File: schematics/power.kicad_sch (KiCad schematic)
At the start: 42 parts, among them J1 9VRMS 60HZ AC, SW1 SW_SPDT, SW2 SW_Push, SW3 SW_Push, SW4 SW_Push, U1 74HC14, U2 LM2576T-ADJ, U3 LM317T, U5 74HC08

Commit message: adjusted some input voltages
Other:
- note added: "+4V5"
- note added: "measured 10V6RMS"
- note added: "~+12V6"
- note removed: "+6V3"
- note removed: "~+10V"
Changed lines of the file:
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@@
 	(generator_version "10.0")
 	(paper "USLetter")
-	(text "~+10V"
+	(text "~+12V6"
 		(exclude_from_sim no)
 		(at 100.33 53.34 0)
@@
 			)
 			(justify left bottom)
+		)
+	)
+	(text "measured 10V6RMS"
+		(exclude_from_sim no)
+		(at 77.47 46.99 0)
+		(effects
+			(font
+				(size 1.27 1.27)
+			)
+			(justify right)
 		)
 	)
@@
 		)
 	)
-	(text "+6V3"
+	(text "+4V5"
 		(exclude_from_sim no)
 		(at 135.89 53.34 0)

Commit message: started a second version
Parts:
- removed C10: 10U, Package_SO:SOIC-8_3.9x4.9mm_P1.27mm, symbol Device:C
- removed C11: 1U, Package_SO:SOIC-8_3.9x4.9mm_P1.27mm, symbol Device:C
- removed C3: 330N, Package_SO:SOIC-8_3.9x4.9mm_P1.27mm, symbol Device:C
- removed C8: 100N, Package_SO:SOIC-8_3.9x4.9mm_P1.27mm, symbol Device:C
- removed D7, D8: 1N4007, Diode_THT:D_DO-35_SOD27_P7.62mm_Horizontal, symbol Diode:1N4148
- removed R36: 22K, symbol Device:R
- removed RV2: 5K, Package_SO:TSSOP-20_4.4x6.5mm_P0.65mm, symbol Device:R_Potentiometer
- removed RV3: 500R, Package_SO:TSSOP-20_4.4x6.5mm_P0.65mm, symbol Device:R_Potentiometer
- removed U3: LM317T, Package_TO_SOT_THT:TO-220-3_Vertical, symbol Regulator_Linear:LM317_TO-220
- added D7, D8: BAT43, Package_SON:WSON-8-1EP_6x5mm_P1.27mm_EP3.4x4mm, symbol Device:D_Schottky
- J1: value 9VRMS 60HZ AC -> 9VRMS 60HZ
- R3: value 47K -> 100K
- R6: value 1K -> 3K3
- R9: value 220R -> 5K6
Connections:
- net +3V3: now also C7.1, L1.2, D7.1 (K)
- net GND: now also D8.2 (A)
- net at R9.2: now also R6.1, U2.4 (FB)
- net at R3.2, U1.13: now also D7.2 (A), D8.1 (K)
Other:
- note added: "60Hz"
- note removed: "+4V5"
- note removed: "measured 10V6RMS"
- note removed: "~+12V6"
- moved on the sheet: C12, C2, C4, C5, C6, C7, C9, D2, D4, D5, D6, D9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

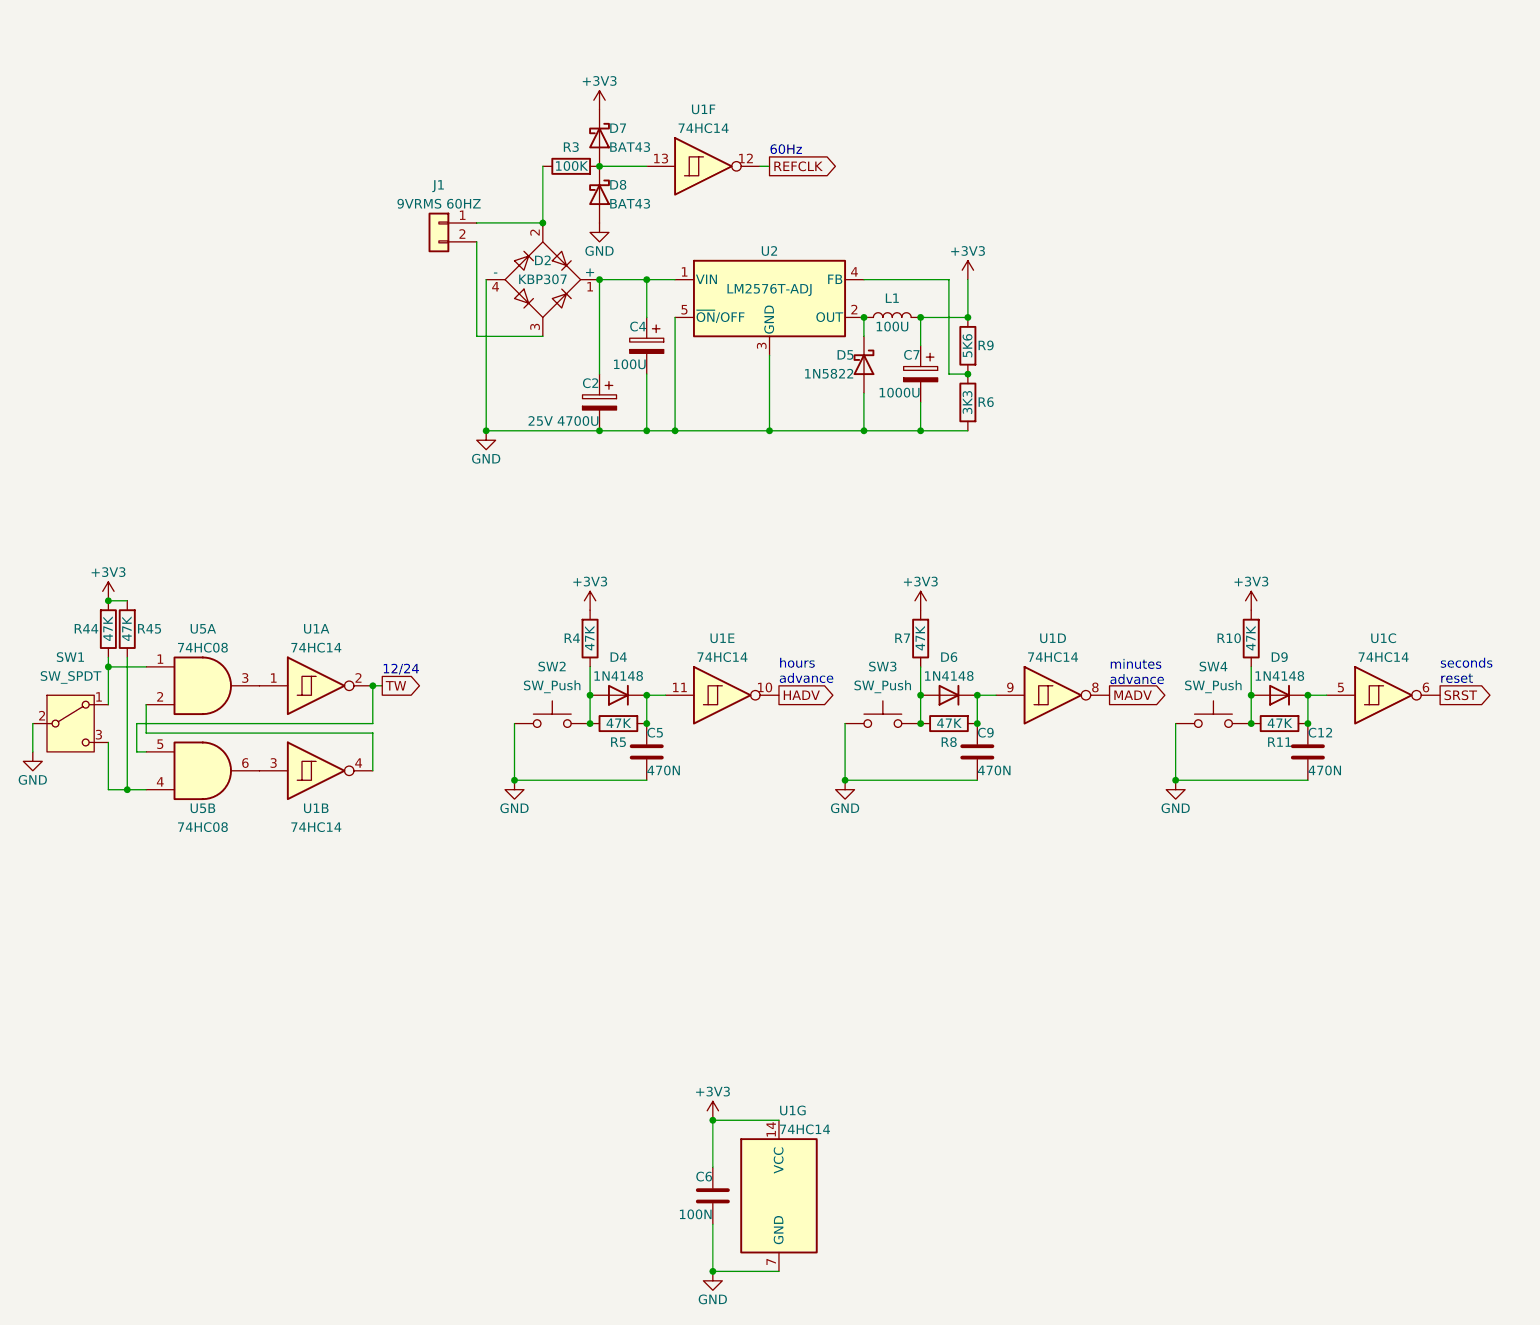
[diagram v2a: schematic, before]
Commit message: switched to diode logic; added LED dimmer
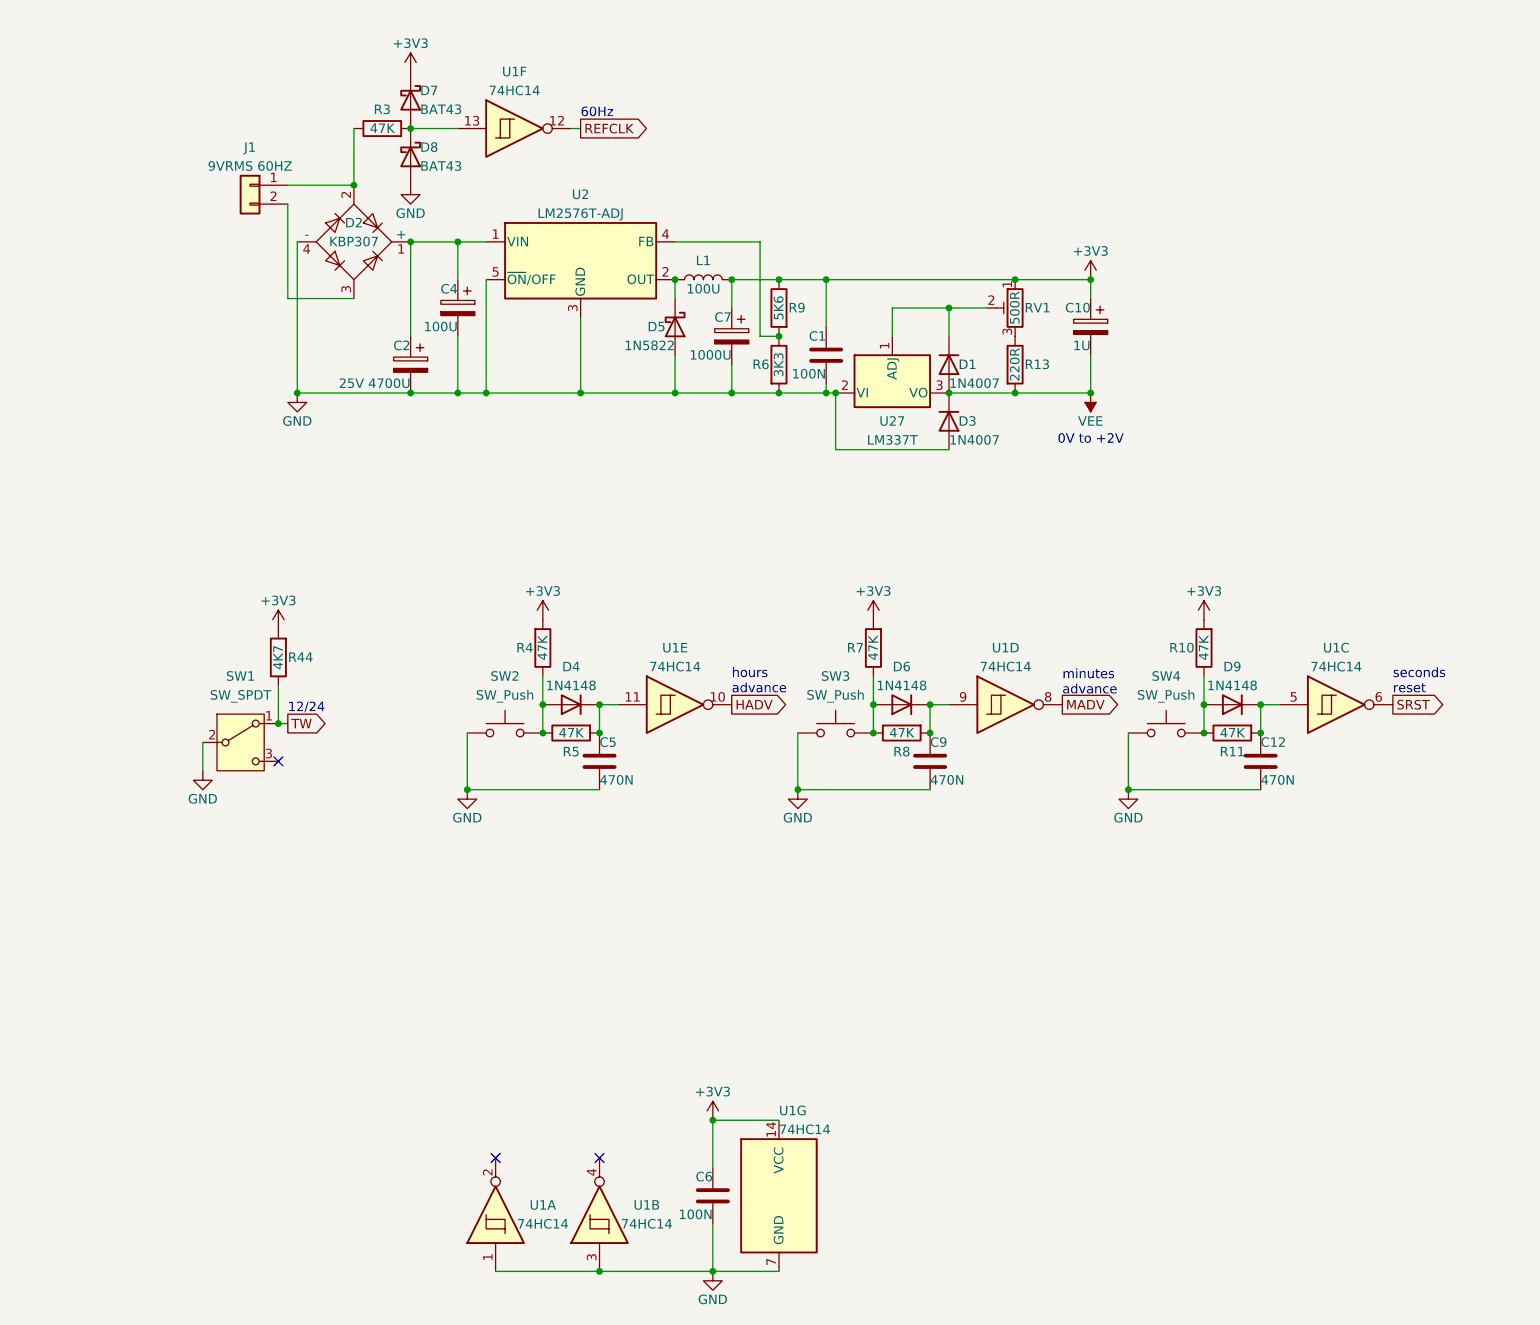
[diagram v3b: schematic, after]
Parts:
- removed R45: 47K, symbol Device:R
- removed U5: 74HC08, Package_TO_SOT_SMD:SC-74A-5_1.55x2.9mm_P0.95mm, symbol 74xx:74LS08
- added C1: 100N, Diode_THT:D_DO-41_SOD81_P10.16mm_Horizontal, symbol Device:C
- added C10: 1U, Package_SO:SOIC-8_3.9x4.9mm_P1.27mm, symbol Device:C_Polarized
- added D1, D3: 1N4007, Diode_THT:D_DO-41_SOD81_P10.16mm_Horizontal, symbol Diode:1N4007
- added R13: 220R, symbol Device:R
- added RV1: 500R, Package_SO:TSSOP-20_4.4x6.5mm_P0.65mm, symbol Device:R_Potentiometer_Trim
- added U27: LM337T, Package_TO_SOT_THT:TO-220-3_Vertical, symbol Regulator_Linear:LM337_TO220
- R3: value 100K -> 47K
- R44: value 47K -> 4K7
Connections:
- net +3V3: now also C1.1, C10.1, RV1.1
- net GND: now also U1.1, U1.3, C1.2, D3.2 (A), U27.2 (VI)
- net TW: now also R44.1, SW1.1 (A); no longer U1.2
- new net: D1.1 (K), RV1.2, U27.1 (ADJ)
- new net: R13.1, RV1.3
- new net VEE: C10.2, D1.2 (A), D3.1 (K), R13.2, U27.3 (VO)
- no-connect marks 0 -> 3
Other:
- note added: "0V to +2V"
- moved on the sheet: C12, C2, C4, C5, C7, C9, D2, D4, D5, D6, D7, D8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

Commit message: re-annotate
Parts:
- renumbered C2 to C1, C4 to C2, C5 to C3, C6 to C4, C7 to C5, C1 to C6, C9 to C7, C10 to C8, C12 to C9, D2 to D1, D7 to D2, D8 to D3, D1 to D7, D3 to D8, R44 to R1, R3 to R2, R4 to R3, R5 to R4, R9 to R5, R13 to R9, U27 to U3
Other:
- moved on the sheet: C8

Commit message: 24-12 converter cleanup
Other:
- note added: "0V to +2V LED dimmer"
- note added: "12/24 select"
- note removed: "0V to +2V"
- note removed: "12/24"
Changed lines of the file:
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@@
 	(generator_version "10.0")
 	(paper "USLetter")
-	(text "0V to +2V"
+	(text "0V to +2V\nLED dimmer"
 		(exclude_from_sim no)
-		(at 191.77 86.36 0)
+		(at 191.77 87.63 0)
 		(effects
 			(font
@@
 		)
 	)
-	(text "12/24"
+	(text "12/24\nselect"
 		(exclude_from_sim no)
 		(at 85.09 123.19 0)

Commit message: added some PCB footprints
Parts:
- removed J1: 9VRMS 60HZ, Connector:Tag-Connect_TC2030-IDC-FP_2x03_P1.27mm_Vertical, symbol Connector_Generic:Conn_01x02
- added J1: 9VRMS_60HZ, Connector_BarrelJack:BarrelJack_Horizontal, symbol Connector:Barrel_Jack_Switch
- C1: footprint Package_SO:SOIC-8_3.9x4.9mm_P1.27mm -> Capacitor_THT:C_Radial_D16.0mm_H25.0mm_P7.50mm
- C2: footprint Package_SO:SOIC-8_3.9x4.9mm_P1.27mm -> Capacitor_THT:C_Radial_D5.0mm_H11.0mm_P2.00mm
- C3, C4, C7, C9: footprint Package_SO:SOIC-8_3.9x4.9mm_P1.27mm -> Capacitor_THT:C_Disc_D5.1mm_W3.2mm_P5.00mm
- C5: footprint Package_SO:SOIC-8_3.9x4.9mm_P1.27mm -> Capacitor_THT:CP_Radial_D10.0mm_P5.00mm
- C6: footprint Diode_THT:D_DO-41_SOD81_P10.16mm_Horizontal -> Capacitor_THT:C_Disc_D5.1mm_W3.2mm_P5.00mm
- C8: footprint Package_SO:SOIC-8_3.9x4.9mm_P1.27mm -> Capacitor_THT:CP_Radial_D5.0mm_P2.00mm
- D1: footprint Diode_THT:Diode_Bridge_DIP-4_W7.62mm_P5.08mm -> Diode_THT:Diode_Bridge_Vishay_KBPM
- D2, D3: footprint Package_SON:WSON-8-1EP_6x5mm_P1.27mm_EP3.4x4mm -> Diode_THT:D_DO-35_SOD27_P7.62mm_Horizontal
- D5: footprint Package_SON:WSON-8-1EP_6x5mm_P1.27mm_EP3.4x4mm -> Diode_THT:D_DO-201_P15.24mm_Horizontal
- L1: footprint Relay_THT:Relay_DPDT_Finder_30.22 -> Inductor_THT:L_Toroid_Vertical_L14.7mm_W8.6mm_P5.58mm_Pulse_KM-1
- R1, R10, R11, R2, R3, R4, R5, R6, R7, R8, R9: footprint (none) -> Resistor_THT:R_Axial_DIN0207_L6.3mm_D2.5mm_P10.16mm_Horizontal
- RV1: footprint Package_SO:TSSOP-20_4.4x6.5mm_P0.65mm -> Potentiometer_THT:Potentiometer_Vishay_T73YP_Vertical
- SW1: footprint Package_SO:SOIC-28W_7.5x17.9mm_P1.27mm -> bvclock:SW_Slide_SPDT
- SW2, SW3, SW4: footprint Package_DFN_QFN:Texas_RVA_VQFN-16-1EP_3.5x3.5mm_P0.5mm_EP2.14x2.14mm_ThermalVias -> bvclock:SW_Push
- U1: footprint Package_SON:WSON-8-1EP_6x5mm_P1.27mm_EP3.4x4mm -> Package_DIP:DIP-14_W7.62mm
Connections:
- net at D1.2, R2.1: now also J1.1
- net at D1.3: now also J1.2
- no-connect marks 3 -> 4
